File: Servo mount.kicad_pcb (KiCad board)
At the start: 2 copper layers, 80 x 35.2 mm, 4 parts, among them M2 VAL**

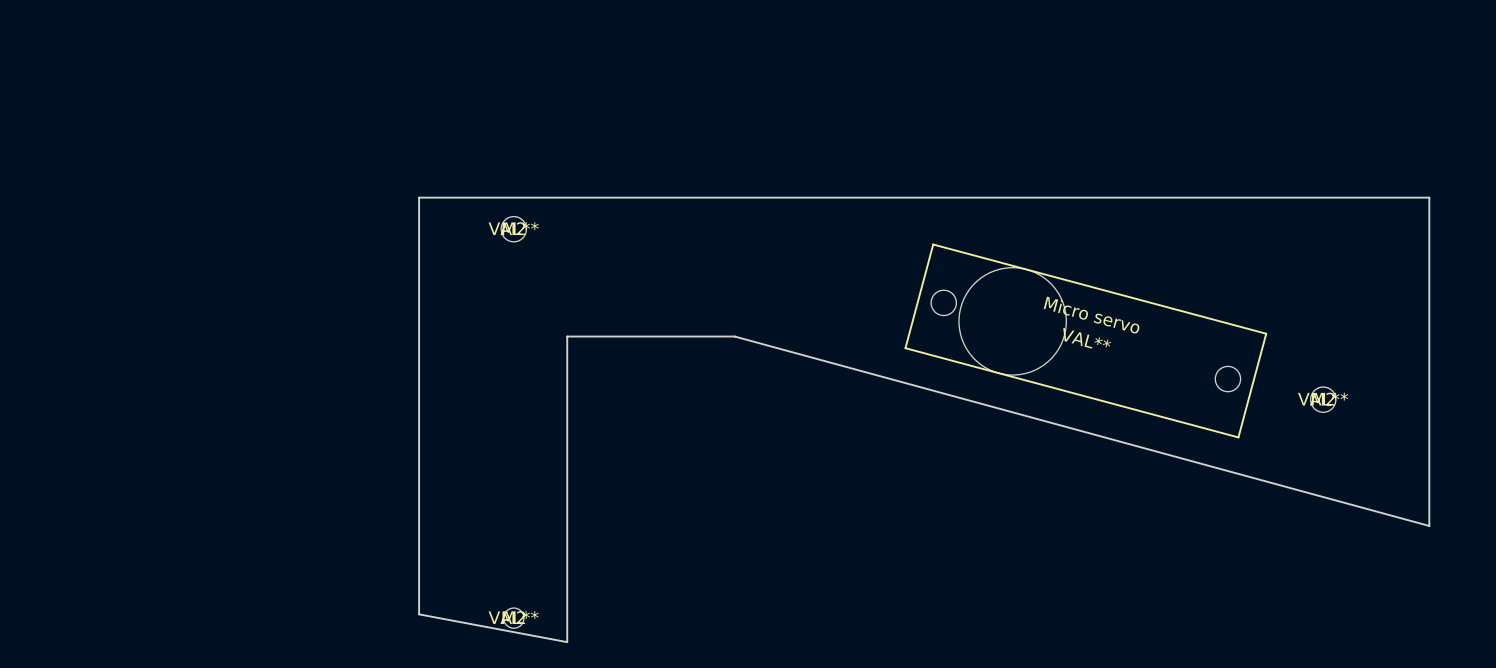
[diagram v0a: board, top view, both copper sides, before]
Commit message: Restored AVR ISP Programming, started PCB layout
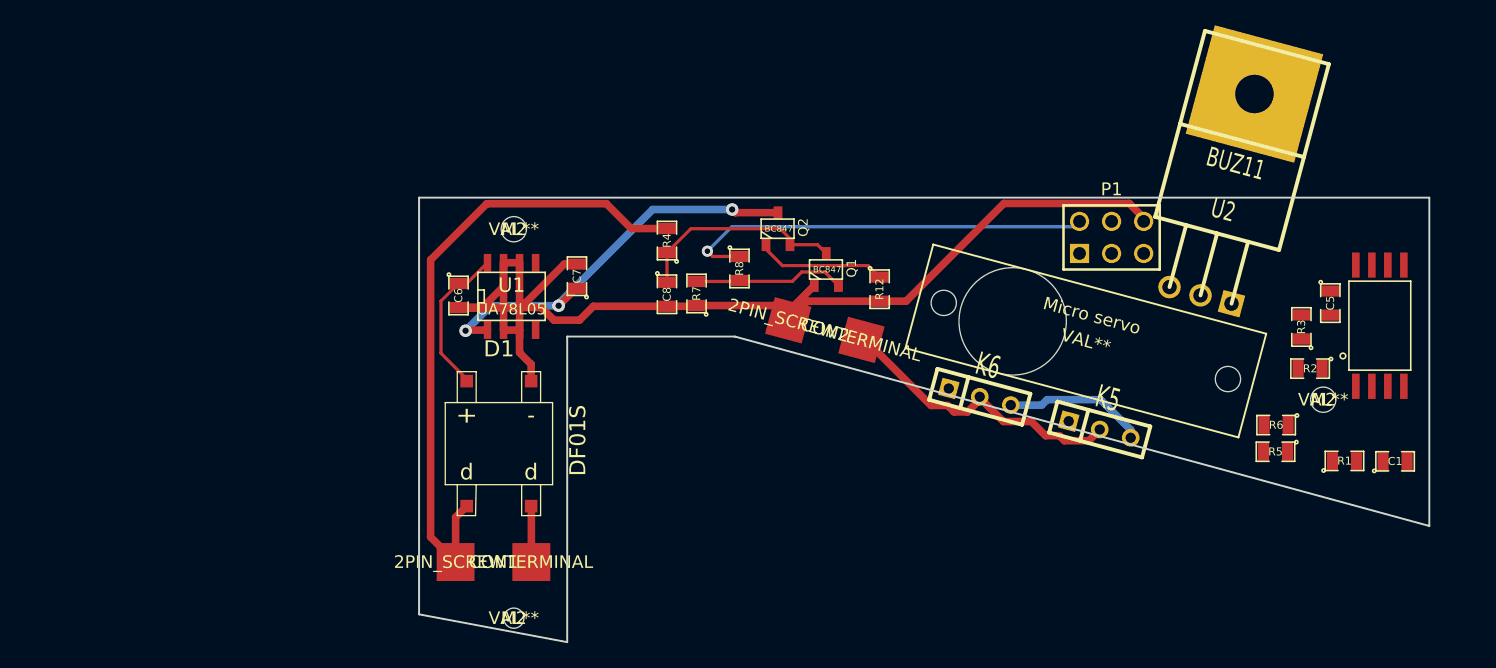
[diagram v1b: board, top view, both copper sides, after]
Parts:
- added C1: 100n, SM0805, F.Cu at (177.3, 120.9)
- added C5: 100n, SM0805, F.Cu at (172.2, 108.3)
- added C6: 100n, SM0805, F.Cu at (103.1, 107.8)
- added C7: 100n, SM0805, F.Cu at (112.5, 106.2)
- added C8: 33p, SM0805, F.Cu at (119.6, 107.7)
- added CON1: 2PIN_SCREWTERMINAL, Solderpad_2, F.Cu at (105.9, 128.9)
- added CON2: 2PIN_SCREWTERMINAL, Solderpad_2, F.Cu at (132.1, 110.5)
- added D1: DF01S, DIPSMD4, F.Cu at (106.3, 119.5)
- added IC1: ATTINY45-S, SOIC-8, F.Cu at (176.1, 110.1)
- added K5: CONN_3, SIL-3, F.Cu at (153.9, 118.4)
- added K6: CONN_3, SIL-3, F.Cu at (144.4, 115.8)
- added P1: CONN_3X2, pin_array_3x2, F.Cu at (154.8, 103.2)
- added Q1: BC847, SOT23, F.Cu at (132.2, 105.7)
- added Q2: BC847, SOT23, F.Cu at (128.4, 102.5)
- added R1: 10k, SM0805, F.Cu at (173.3, 120.8)
- added R12: 4k7, SM0805, F.Cu at (136.5, 107.2)
- added R2: 1k, SM0805, F.Cu at (170.6, 113.5)
- added R3: 10k, SM0805, F.Cu at (169.9, 110.2)
- added R4: 10k, SM0805, F.Cu at (119.6, 103.4)
- added R5: 1k, SM0805, F.Cu at (167.8, 120.1)
- added R6: 1k, SM0805, F.Cu at (167.9, 118.0)
- added R7: 10k, SM0805, F.Cu at (122.0, 107.6)
- added R8: 1k, SM0805, F.Cu at (125.4, 105.6)
- added U1: UA78L05, SO8E, F.Cu at (107.3, 107.8)
- added U2: BUZ11, TO220GDS, F.Cu at (161.9, 107.7)
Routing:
- net GND: track 0.00 -> 98.4 mm
- net VAA: track 0.00 -> 50.9 mm
- net DIS_SIGNAL: track 0.00 -> 33.2 mm, vias 0 -> 1
- net +5V: track 0.00 -> 32.7 mm, vias 0 -> 3
- net VCC: track 0.00 -> 23.7 mm
- net N-0000010: track 0.00 -> 16.8 mm
- net N-000009: track 0.00 -> 12.1 mm
- net N-0000012: track 0.00 -> 12.0 mm
- net AGND: track 0.00 -> 11.3 mm
- net Rail signal: track 0.00 -> 10.3 mm
- net -VAA: track 0.00 -> 4.44 mm
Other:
- net class Power added: clearance 0.254, trace_width 0.6, via_dia 1, via_drill 0.635

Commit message: Layed out board
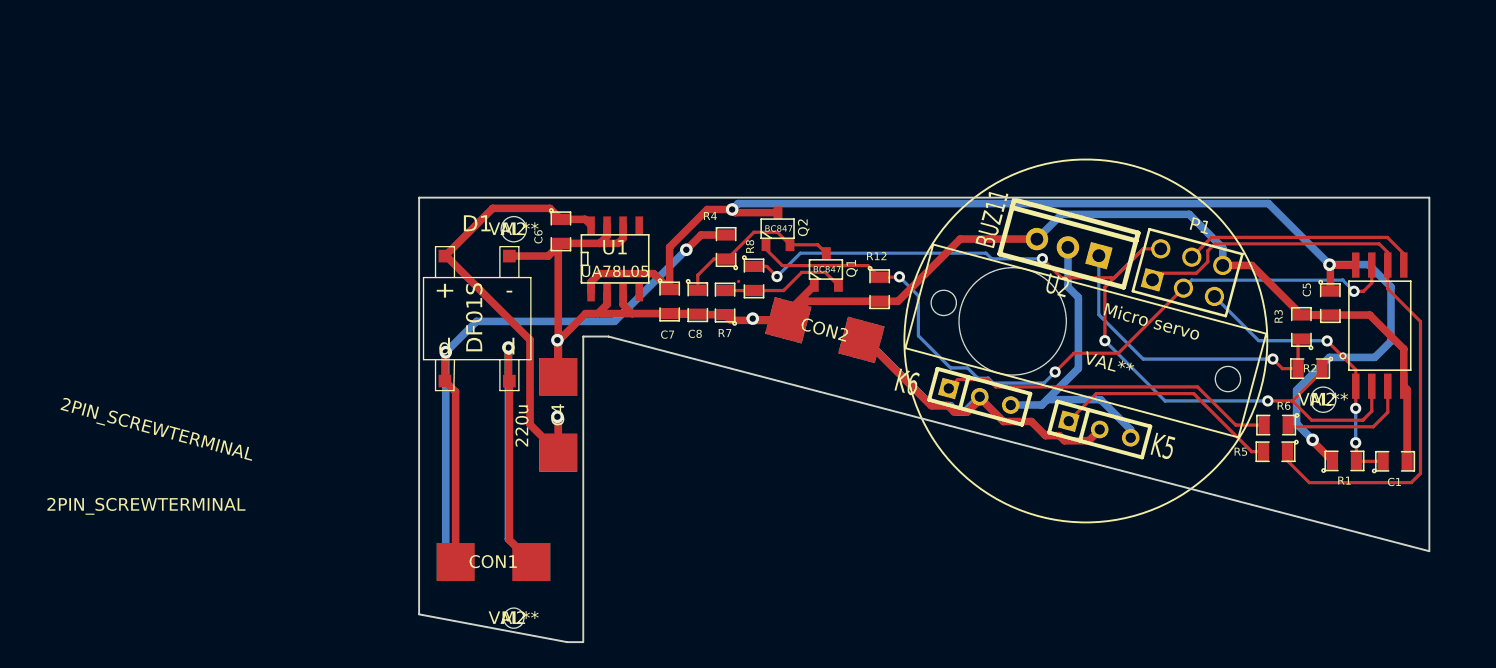
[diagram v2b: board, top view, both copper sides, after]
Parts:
- added C4: 220u, Solderpad_2, F.Cu at (111.0, 117.2)
- U2: footprint TO220GDS -> TO220_VERT
- moved U2 11.2 mm to (151.4, 103.9)
- moved D1 10.0 mm to (104.6, 109.6)
- moved C6 9.57 mm to (111.2, 102.7)
- moved U1 8.72 mm to (115.5, 104.8)
- moved C7 7.61 mm to (119.8, 108.2), turned to 270 degrees
- moved P1 6.64 mm to (160.9, 105.9), turned to 345 degrees
- moved R4 4.71 mm to (124.3, 103.9)
- moved C8 2.52 mm to (122.1, 108.3)
- moved R7 2.37 mm to (124.2, 108.3)
- moved R8 1.40 mm to (126.5, 106.4)
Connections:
- IC1 pad 2: GND FET -> DIS_SIGNAL
- IC1 pad 5: DIS_SIGNAL -> MOSI
- IC1 pad 6: PB3 -> MISO
- P1 pad 1: (no net) -> MISO
- P1 pad 3: (no net) -> Rail signal
- P1 pad 4: (no net) -> MOSI
- R2 pad 1: GND FET -> DIS_SIGNAL
- R5 pad 1: PB3 -> MISO
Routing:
- net +5V: track 32.7 -> 100.6 mm
- net MISO: track 0.00 -> 51.4 mm
- net Rail signal: track 10.3 -> 60.0 mm, vias 0 -> 3
- net DIS_SIGNAL: track 33.2 -> 73.3 mm, vias 1 -> 4
- net GND: track 98.4 -> 135.3 mm, vias 0 -> 2
- net -VAA: track 4.44 -> 35.5 mm, vias 0 -> 1
- net N-000002: track 0.00 -> 26.8 mm
- net N-000006: track 12.1 -> 38.8 mm, vias 0 -> 1
- net N-000007: track 0.00 -> 24.7 mm, vias 0 -> 1
- net N-0000012: track 0.00 -> 23.0 mm, vias 0 -> 3
- net MOSI: track 0.00 -> 18.9 mm
- net N-000003: track 0.00 -> 18.2 mm
- net AGND: track 11.3 -> 24.7 mm
- net VCC: track 23.7 -> 36.0 mm
- net PB4: track 0.00 -> 10.5 mm
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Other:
- outline, holes or cut-outs redrawn

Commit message: Rev. 0  as send to OSHPark
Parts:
- added ?: , dp_devices-CC-BY-SA, B.Cu at (163.9, 100.4)
- added P2: CONN_2, SIL-2, F.Cu at (177.0, 119.0)
- IC1: value ATTINY45-S -> ATTINY84-SS; footprint SOIC-8 -> SOIC-14
- moved R2 4.37 mm to (173.6, 116.7)
- moved C5 4.09 mm to (168.2, 107.3), turned to 90 degrees
- moved IC1 3.10 mm to (173.9, 107.9)
- moved R3 3.07 mm to (168.1, 112.7)
- moved R5 2.34 mm to (168.1, 122.5)
- moved R1 2.17 mm to (173.3, 123.0)
- moved C1 2.17 mm to (177.3, 123.0)
- moved R6 2.13 mm to (168.0, 120.1)
- moved M2 2.08 mm to (170.4, 117.7)
- moved D1 1.27 mm to (104.5, 110.8)
- moved M2 0.40 mm to (107.5, 132.9)
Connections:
- C1 pad 1: N-0000012 -> Reset
- IC1 pad 1: N-0000012 -> +5V
- IC1 pad 2: DIS_SIGNAL -> PB3
- IC1 pad 4: GND -> N-0000015
- IC1 pad 5: MOSI -> Rail signal
- IC1 pad 6: MISO -> GND FET
- IC1 pad 7: Rail signal -> MOSI
- IC1 pad 8: +5V -> MISO
- P1 pad 3: Rail signal -> SCK
- P1 pad 5: N-0000012 -> Reset
- R1 pad 2: N-0000012 -> Reset
- R2 pad 1: DIS_SIGNAL -> GND FET
- R5 pad 1: MISO -> PB3
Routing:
- net GND: track 135.3 -> 196.8 mm, vias 2 -> 4
- net Reset: track 0.00 -> 27.6 mm
- net MISO: track 51.4 -> 24.8 mm, vias 0 -> 1
- net SCK: track 0.00 -> 24.5 mm, vias 0 -> 2
- net N-0000012: track 23.0 -> 0.00 mm, vias 3 -> 0
- net DIS_SIGNAL: track 73.3 -> 56.2 mm, vias 4 -> 2
- net N-0000015: track 0.00 -> 16.8 mm
- net PB3: track 0.00 -> 15.1 mm, vias 0 -> 2
- net GND FET: track 0.00 -> 4.73 mm
- net +5V: track 100.6 -> 96.4 mm, vias 3 -> 4
- net -VAA: track 35.5 -> 39.4 mm
- net VAA: track 60.0 -> 63.6 mm
- net MOSI: track 18.9 -> 22.5 mm, vias 0 -> 1
- net N-000007: track 24.7 -> 26.7 mm
- net N-0000022: track 38.8 -> 40.3 mm
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- added copper zone on B.Cu, net GND
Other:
- board text added: "B"
- board text added: "Designed by: Dirkjan Krijnders https://github.com/dirkjankrijnders/Servo_mount"
- board text added: "GND"
- board text added: "R"
- board text added: "Rail"
- board text added: "Servo power"

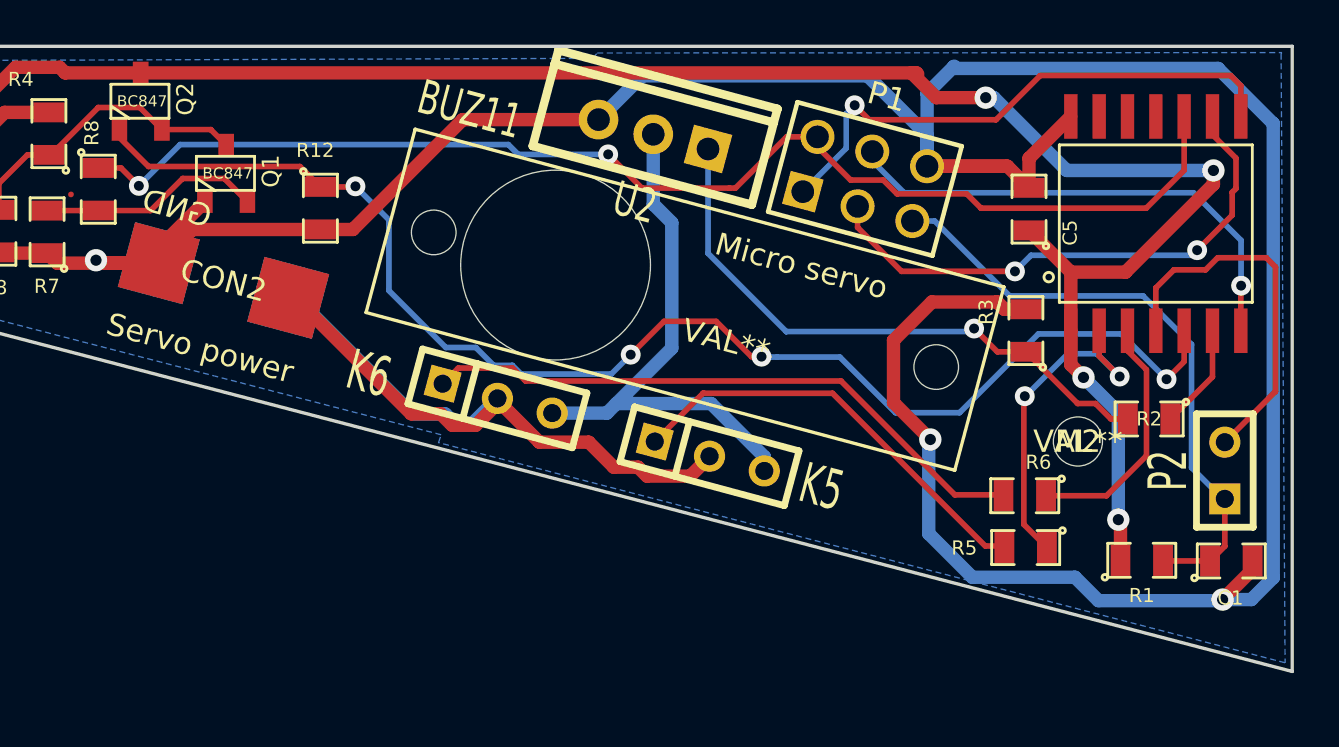
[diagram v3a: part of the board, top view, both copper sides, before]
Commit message: Changed SOIC-14w to SOIC-14
Close #3
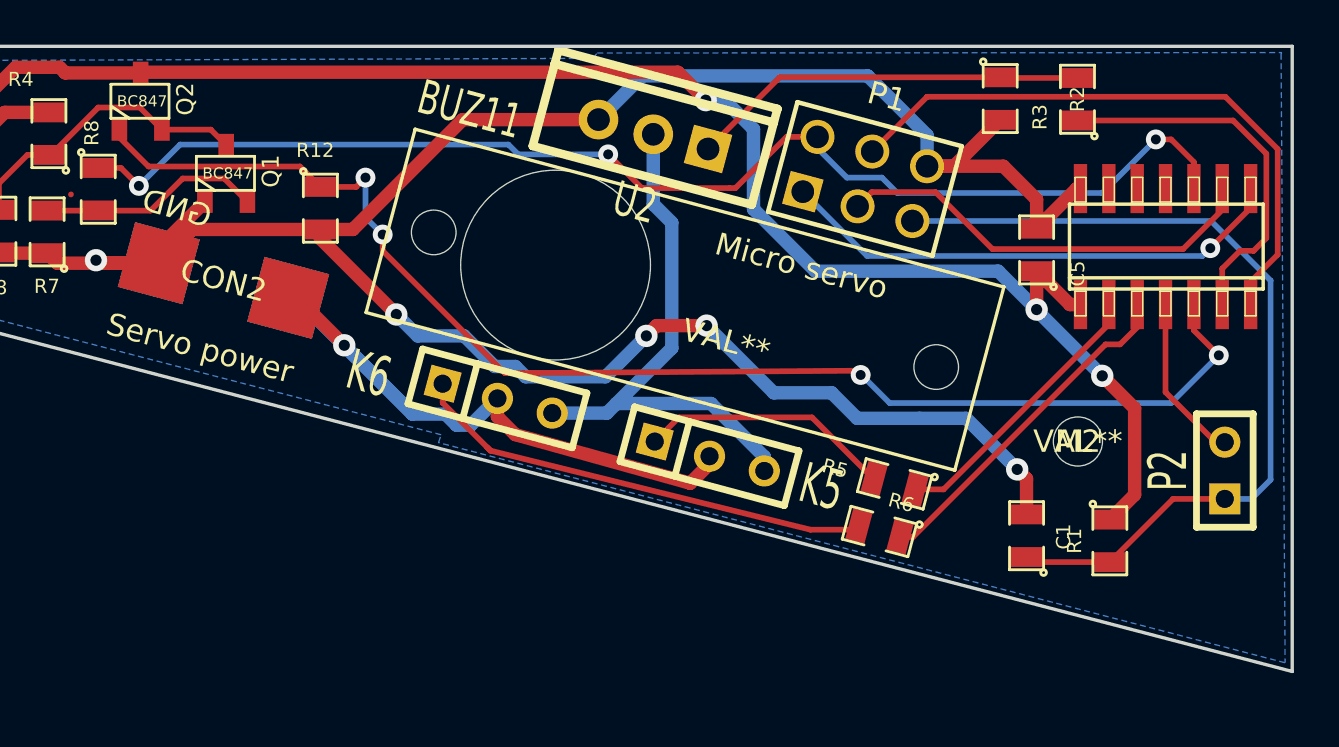
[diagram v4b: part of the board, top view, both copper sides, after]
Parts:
- moved R2 14.7 mm to (170.4, 102.4), turned to 90 degrees
- moved R3 10.5 mm to (166.9, 102.3), turned to 270 degrees
- moved C1 9.24 mm to (168.1, 121.9), turned to 90 degrees
- moved R6 6.70 mm to (161.5, 121.7), turned to 165 degrees
- moved R5 6.53 mm to (162.2, 119.6), turned to 165 degrees
- moved C5 1.86 mm to (168.6, 109.1)
- moved R1 1.67 mm to (171.8, 122.2), turned to 270 degrees
- moved IC1 1.11 mm to (174.3, 109.0)
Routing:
- net GND: track 196.8 -> 161.2 mm, vias 4 -> 6
- net +5V: track 96.4 -> 83.8 mm, vias 4 -> 3
- net GND FET: track 4.73 -> 17.0 mm
- net Reset: track 27.6 -> 38.6 mm
- net N-0000015: track 16.8 -> 7.51 mm
- net N-000007: track 26.7 -> 17.9 mm, vias 1 -> 0
- net N-000002: track 19.5 -> 11.4 mm
- net N-000001: track 27.8 -> 21.1 mm
- net SCK: track 24.5 -> 19.3 mm, vias 2 -> 0
- net MOSI: track 22.5 -> 27.6 mm, vias 1 -> 0
- net VCC: track 36.0 -> 31.6 mm, vias 0 -> 1
- net PB4: track 11.2 -> 15.5 mm
- net PB3: track 15.1 -> 12.6 mm, vias 2 -> 0
- net MISO: track 24.8 -> 23.0 mm
- net Rail signal: track 61.0 -> 60.0 mm
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
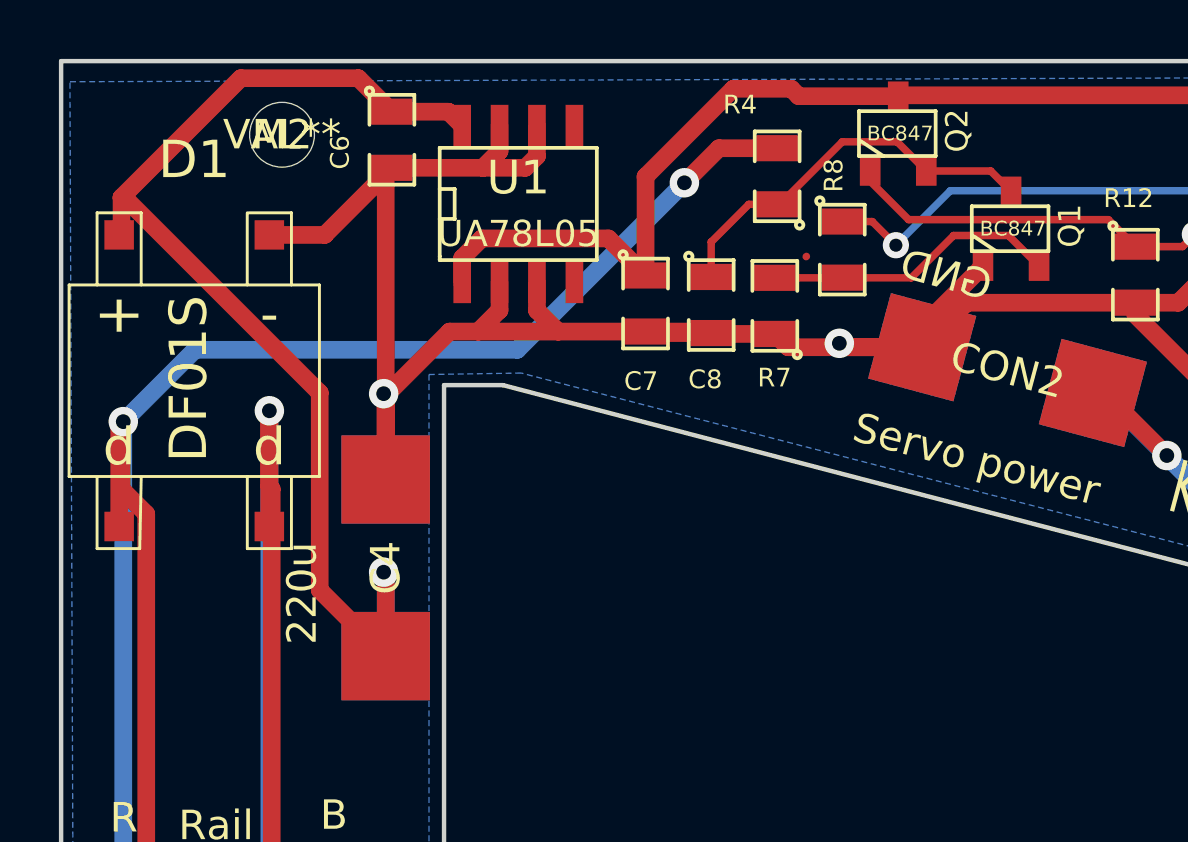
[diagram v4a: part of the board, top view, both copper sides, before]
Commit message: Fixed rectifier pinout, added front ground plane, closes #2
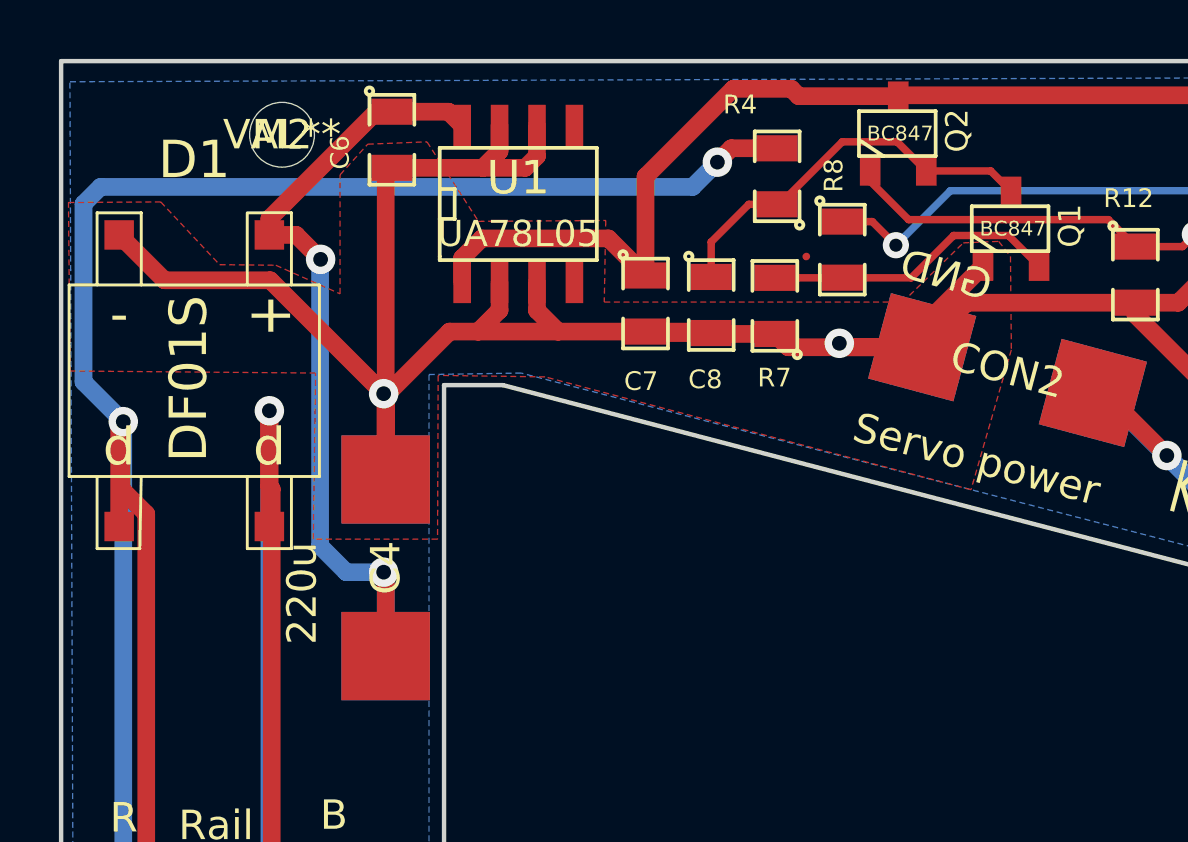
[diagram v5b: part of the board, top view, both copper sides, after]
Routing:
- net N-0000022: track 40.3 -> 28.9 mm, vias 1 -> 2
- net VAA: track 63.6 -> 69.8 mm
- net GND: track 161.2 -> 167.3 mm
- added copper zone on F.Cu, net GND
